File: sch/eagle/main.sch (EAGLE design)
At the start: 19 parts, among them IC1 LM339N

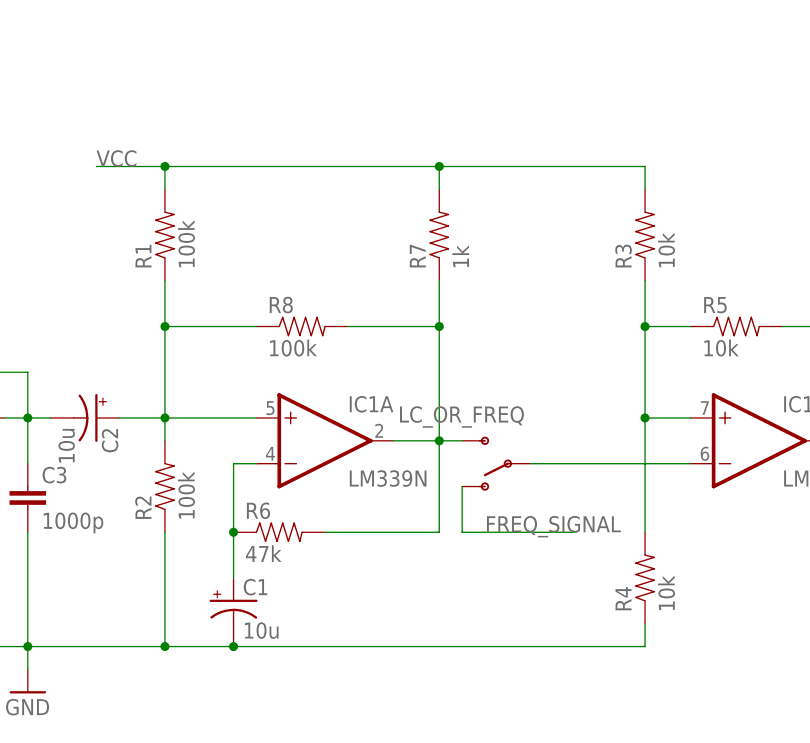
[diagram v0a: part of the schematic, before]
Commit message: [ update ] add missing power connections to lm339
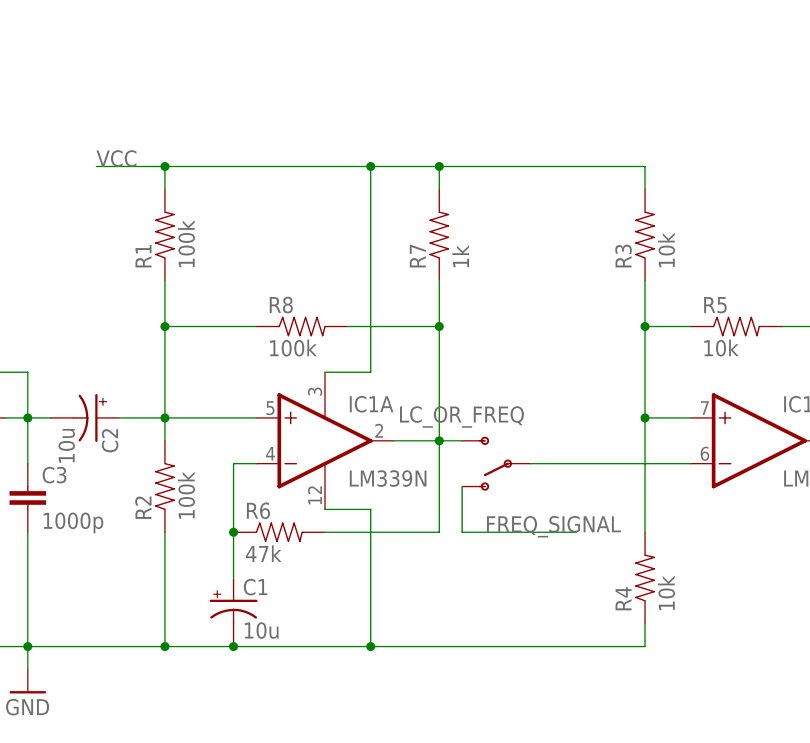
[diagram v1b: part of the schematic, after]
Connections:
- net GND: now also IC1P.GND
- net VCC: now also IC1P.V+
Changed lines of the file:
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@@
 <instance part="FREQ_CON" gate="G$1" x="0" y="93.98"/>
 <instance part="OSC_OUT" gate="G$1" x="0" y="81.28"/>
+<instance part="IC1" gate="P" x="83.82" y="66.04"/>
 </instances>
 <busses>
@@
 <pinref part="GND2" gate="1" pin="GND"/>
 <wire x1="50.8" y1="43.18" x2="50.8" y2="40.64" width="0.1524" layer="91"/>
-<wire x1="73.66" y1="43.18" x2="119.38" y2="43.18" width="0.1524" layer="91"/>
+<wire x1="73.66" y1="43.18" x2="88.9" y2="43.18" width="0.1524" layer="91"/>
 <junction x="73.66" y="43.18"/>
 <pinref part="R4" gate="G$1" pin="1"/>
+<wire x1="88.9" y1="43.18" x2="119.38" y2="43.18" width="0.1524" layer="91"/>
 <wire x1="119.38" y1="45.72" x2="119.38" y2="43.18" width="0.1524" layer="91"/>
+<pinref part="IC1" gate="P" pin="GND"/>
+<wire x1="83.82" y1="58.42" x2="88.9" y2="58.42" width="0.1524" layer="91"/>
+<wire x1="88.9" y1="58.42" x2="88.9" y2="43.18" width="0.1524" layer="91"/>
+<junction x="88.9" y="43.18"/>
 </segment>
 </net>
@@
 <wire x1="66.04" y1="96.52" x2="58.42" y2="96.52" width="0.1524" layer="91"/>
 <label x="58.42" y="96.52" size="1.778" layer="95"/>
-<wire x1="66.04" y1="96.52" x2="96.52" y2="96.52" width="0.1524" layer="91"/>
+<wire x1="66.04" y1="96.52" x2="88.9" y2="96.52" width="0.1524" layer="91"/>
 <junction x="66.04" y="96.52"/>
 <pinref part="R7" gate="G$1" pin="2"/>
+<wire x1="88.9" y1="96.52" x2="96.52" y2="96.52" width="0.1524" layer="91"/>
 <wire x1="96.52" y1="96.52" x2="96.52" y2="93.98" width="0.1524" layer="91"/>
 <wire x1="96.52" y1="96.52" x2="119.38" y2="96.52" width="0.1524" layer="91"/>
@@
 <pinref part="R3" gate="G$1" pin="2"/>
 <wire x1="119.38" y1="96.52" x2="119.38" y2="93.98" width="0.1524" layer="91"/>
+<pinref part="IC1" gate="P" pin="V+"/>
+<wire x1="83.82" y1="73.66" x2="88.9" y2="73.66" width="0.1524" layer="91"/>
+<wire x1="88.9" y1="73.66" x2="88.9" y2="96.52" width="0.1524" layer="91"/>
+<junction x="88.9" y="96.52"/>
 </segment>
 </net>

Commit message: [ update ] eagle, mcu_con
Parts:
- removed OSC_OUT: M01PTH, SparkFun:M01PTH
- added MCU_CON: (no value), SparkFun:M02PTH
- renumbered LC_OR_FREQ to FREQ_SWITCH, L_OR_C to LC_SWITCH
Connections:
- removed net LC_SENSE: LC_SWITCH.6
- removed net OSC_OUT: IC1B.OUT, OSC_OUT.1, R5.2
- new net MCU_FREQ: IC1B.OUT, MCU_CON.2, R5.2
- new net MCU_LC_SENSE: LC_SWITCH.6, MCU_CON.1
- net C: now also C2.-, C3.1, L1.2, LC_SWITCH.1; no longer L1.1, LC_SWITCH.3, LC_SWITCH.4
- net L: now also L1.1, LC_SWITCH.3, LC_SWITCH.4; no longer C2.-, C3.1, L1.2, LC_SWITCH.1
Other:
- note removed: "arduino pin2"
- note removed: "arduino pin5"
- moved on the sheet: FREQ_CON, POWER_CON
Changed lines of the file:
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@@
 <part name="C3" library="SparkFun" deviceset="CAP" device="KIT" value="1000p"/>
 <part name="L1" library="rcl" deviceset="L-EU" device="0207/10" value="221u"/>
-<part name="LC_OR_FREQ" library="SparkFun" deviceset="SWITCH-SPST" device="PTH"/>
-<part name="L_OR_C" library="SparkFun" deviceset="SWITCH-DPDT" device="EG2211"/>
+<part name="FREQ_SWITCH" library="SparkFun" deviceset="SWITCH-SPST" device="PTH"/>
+<part name="LC_SWITCH" library="SparkFun" deviceset="SWITCH-DPDT" device="EG2211"/>
 <part name="GND1" library="SparkFun" deviceset="GND" device=""/>
 <part name="SUPPLY1" library="supply2" deviceset="VCC" device=""/>
@@
 <part name="GND2" library="SparkFun" deviceset="GND" device=""/>
 <part name="FREQ_CON" library="SparkFun" deviceset="M01" device="PTH"/>
-<part name="OSC_OUT" library="SparkFun" deviceset="M01" device="PTH"/>
+<part name="MCU_CON" library="SparkFun" deviceset="M02" device="PTH"/>
 </parts>
 <sheets>
 <sheet>
 <plain>
-<text x="27.94" y="58.42" size="1.778" layer="91">arduino pin2</text>
-<text x="149.86" y="60.96" size="1.778" layer="91">arduino pin5</text>
 </plain>
 <instances>
@@
 <instance part="C3" gate="G$1" x="50.8" y="58.42"/>
 <instance part="L1" gate="G$1" x="43.18" y="68.58" rot="R90"/>
-<instance part="LC_OR_FREQ" gate="1" x="104.14" y="63.5" rot="R180"/>
-<instance part="L_OR_C" gate="G$1" x="17.78" y="68.58"/>
-<instance part="GND1" gate="1" x="15.24" y="101.6"/>
-<instance part="SUPPLY1" gate="G$1" x="15.24" y="109.22"/>
-<instance part="POWER_CON" gate="G$1" x="0" y="104.14"/>
+<instance part="FREQ_SWITCH" gate="1" x="104.14" y="63.5" rot="R180"/>
+<instance part="LC_SWITCH" gate="G$1" x="17.78" y="68.58"/>
+<instance part="GND1" gate="1" x="15.24" y="109.22"/>
+<instance part="SUPPLY1" gate="G$1" x="15.24" y="116.84"/>
+<instance part="POWER_CON" gate="G$1" x="0" y="111.76"/>
 <instance part="LC_CON" gate="G$1" x="0" y="66.04"/>
 <instance part="R8" gate="G$1" x="81.28" y="78.74"/>
 <instance part="GND2" gate="1" x="50.8" y="38.1"/>
-<instance part="FREQ_CON" gate="G$1" x="0" y="93.98"/>
-<instance part="OSC_OUT" gate="G$1" x="0" y="81.28"/>
+<instance part="FREQ_CON" gate="G$1" x="0" y="83.82"/>
 <instance part="IC1" gate="P" x="83.82" y="66.04"/>
+<instance part="MCU_CON" gate="G$1" x="0" y="96.52"/>
 </instances>
 <busses>
@@
 <segment>
 <pinref part="POWER_CON" gate="G$1" pin="1"/>
-<wire x1="7.62" y1="104.14" x2="15.24" y2="104.14" width="0.1524" layer="91"/>
+<wire x1="7.62" y1="111.76" x2="15.24" y2="111.76" width="0.1524" layer="91"/>
 <pinref part="GND1" gate="1" pin="GND"/>
 </segment>
@@
 <pinref part="LC_CON" gate="G$1" pin="1"/>
 <wire x1="7.62" y1="66.04" x2="7.62" y2="63.5" width="0.1524" layer="91"/>
-<pinref part="L_OR_C" gate="G$1" pin="5"/>
+<pinref part="LC_SWITCH" gate="G$1" pin="5"/>
 <wire x1="7.62" y1="63.5" x2="12.7" y2="63.5" width="0.1524" layer="91"/>
 <wire x1="7.62" y1="63.5" x2="7.62" y2="43.18" width="0.1524" layer="91"/>
@@
 <pinref part="POWER_CON" gate="G$1" pin="2"/>
 <pinref part="SUPPLY1" gate="G$1" pin="VCC"/>
-<wire x1="7.62" y1="106.68" x2="15.24" y2="106.68" width="0.1524" layer="91"/>
+<wire x1="7.62" y1="114.3" x2="15.24" y2="114.3" width="0.1524" layer="91"/>
 </segment>
 <segment>
@@
 <net name="C" class="0">
 <segment>
-<pinref part="L_OR_C" gate="G$1" pin="3"/>
-<wire x1="22.86" y1="68.58" x2="25.4" y2="68.58" width="0.1524" layer="91"/>
-<wire x1="25.4" y1="68.58" x2="25.4" y2="66.04" width="0.1524" layer="91"/>
-<pinref part="L_OR_C" gate="G$1" pin="4"/>
-<wire x1="25.4" y1="66.04" x2="22.86" y2="66.04" width="0.1524" layer="91"/>
-<pinref part="L1" gate="G$1" pin="1"/>
-<wire x1="25.4" y1="68.58" x2="38.1" y2="68.58" width="0.1524" layer="91"/>
-<junction x="25.4" y="68.58"/>
-<label x="22.86" y="68.58" size="1.778" layer="95"/>
-</segment>
-</net>
-<net name="L" class="0">
-<segment>
 <pinref part="L1" gate="G$1" pin="2"/>
 <pinref part="C2" gate="G$1" pin="-"/>
@@
 <wire x1="50.8" y1="63.5" x2="50.8" y2="68.58" width="0.1524" layer="91"/>
 <junction x="50.8" y="68.58"/>
-<pinref part="L_OR_C" gate="G$1" pin="1"/>
+<pinref part="LC_SWITCH" gate="G$1" pin="1"/>
 <wire x1="22.86" y1="73.66" x2="50.8" y2="73.66" width="0.1524" layer="91"/>
 <wire x1="50.8" y1="73.66" x2="50.8" y2="68.58" width="0.1524" layer="91"/>
@@
 <pinref part="LC_CON" gate="G$1" pin="2"/>
 <wire x1="7.62" y1="68.58" x2="7.62" y2="71.12" width="0.1524" layer="91"/>
-<pinref part="L_OR_C" gate="G$1" pin="2"/>
+<pinref part="LC_SWITCH" gate="G$1" pin="2"/>
 <wire x1="7.62" y1="71.12" x2="12.7" y2="71.12" width="0.1524" layer="91"/>
-</segment>
-</net>
-<net name="LC_SENSE" class="0">
-<segment>
-<pinref part="L_OR_C" gate="G$1" pin="6"/>
-<wire x1="22.86" y1="60.96" x2="33.02" y2="60.96" width="0.1524" layer="91"/>
-<label x="27.94" y="60.96" size="1.778" layer="95"/>
 </segment>
 </net>
@@
 <wire x1="96.52" y1="55.88" x2="96.52" y2="66.04" width="0.1524" layer="91"/>
 <junction x="96.52" y="66.04"/>
-<pinref part="LC_OR_FREQ" gate="1" pin="S"/>
+<pinref part="FREQ_SWITCH" gate="1" pin="S"/>
 <wire x1="96.52" y1="66.04" x2="99.06" y2="66.04" width="0.1524" layer="91"/>
 </segment>
@@
 <segment>
 <pinref part="FREQ_CON" gate="G$1" pin="1"/>
-<wire x1="7.62" y1="93.98" x2="15.24" y2="93.98" width="0.1524" layer="91"/>
-<label x="7.62" y="93.98" size="1.778" layer="95"/>
+<wire x1="7.62" y1="83.82" x2="15.24" y2="83.82" width="0.1524" layer="91"/>
+<label x="7.62" y="83.82" size="1.778" layer="95"/>
 </segment>
 <segment>
 <pinref part="IC1" gate="B" pin="-IN"/>
 <wire x1="106.68" y1="63.5" x2="124.46" y2="63.5" width="0.1524" layer="91"/>
-<pinref part="LC_OR_FREQ" gate="1" pin="P"/>
-</segment>
-<segment>
-<pinref part="LC_OR_FREQ" gate="1" pin="O"/>
+<pinref part="FREQ_SWITCH" gate="1" pin="P"/>
+</segment>
+<segment>
+<pinref part="FREQ_SWITCH" gate="1" pin="O"/>
 <wire x1="99.06" y1="60.96" x2="99.06" y2="55.88" width="0.1524" layer="91"/>
 <wire x1="99.06" y1="55.88" x2="111.76" y2="55.88" width="0.1524" layer="91"/>
@@
 </segment>
 </net>
-<net name="OSC_OUT" class="0">
-<segment>
-<pinref part="OSC_OUT" gate="G$1" pin="1"/>
-<wire x1="7.62" y1="81.28" x2="15.24" y2="81.28" width="0.1524" layer="91"/>
-<label x="7.62" y="81.28" size="1.778" layer="95"/>
-</segment>
+<net name="MCU_FREQ" class="0">
 <segment>
 <pinref part="R5" gate="G$1" pin="2"/>
@@
 <label x="147.32" y="66.04" size="1.778" layer="95"/>
 </segment>
-</net>
+<segment>
+<pinref part="MCU_CON" gate="G$1" pin="2"/>
+<wire x1="7.62" y1="99.06" x2="15.24" y2="99.06" width="0.1524" layer="91"/>
+<label x="7.62" y="99.06" size="1.778" layer="95"/>
+</segment>
+</net>
+<net name="MCU_LC_SENSE" class="0">
+<segment>
+<pinref part="LC_SWITCH" gate="G$1" pin="6"/>
+<wire x1="22.86" y1="60.96" x2="33.02" y2="60.96" width="0.1524" layer="91"/>
+<label x="27.94" y="60.96" size="1.778" layer="95"/>
+</segment>
+<segment>
+<pinref part="MCU_CON" gate="G$1" pin="1"/>
+<wire x1="7.62" y1="96.52" x2="15.24" y2="96.52" width="0.1524" layer="91"/>
+<label x="7.62" y="96.52" size="1.778" layer="95"/>
+</segment>
+</net>
+<net name="L" class="0">
+<segment>
+<pinref part="LC_SWITCH" gate="G$1" pin="3"/>
+<wire x1="22.86" y1="68.58" x2="25.4" y2="68.58" width="0.1524" layer="91"/>
+<wire x1="25.4" y1="68.58" x2="25.4" y2="66.04" width="0.1524" layer="91"/>
+<pinref part="LC_SWITCH" gate="G$1" pin="4"/>
+<wire x1="25.4" y1="66.04" x2="22.86" y2="66.04" width="0.1524" layer="91"/>
+<pinref part="L1" gate="G$1" pin="1"/>
+<wire x1="25.4" y1="68.58" x2="38.1" y2="68.58" width="0.1524" layer="91"/>
+<junction x="25.4" y="68.58"/>
+<label x="22.86" y="68.58" size="1.778" layer="95"/>
+</segment>
+</net>

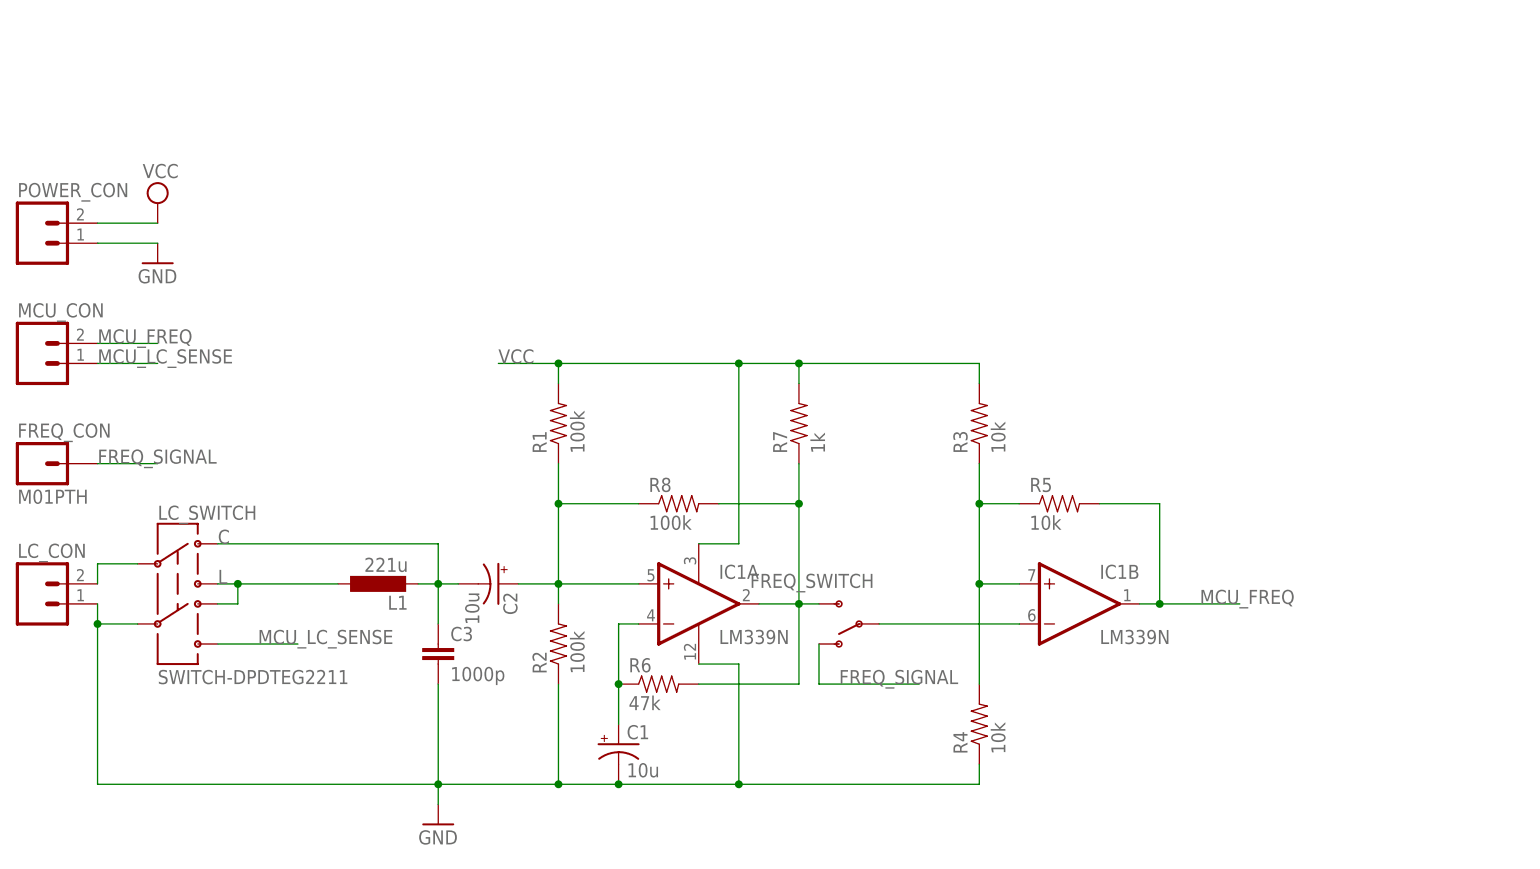
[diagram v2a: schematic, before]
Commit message: [ update ] eagle, switch connectors
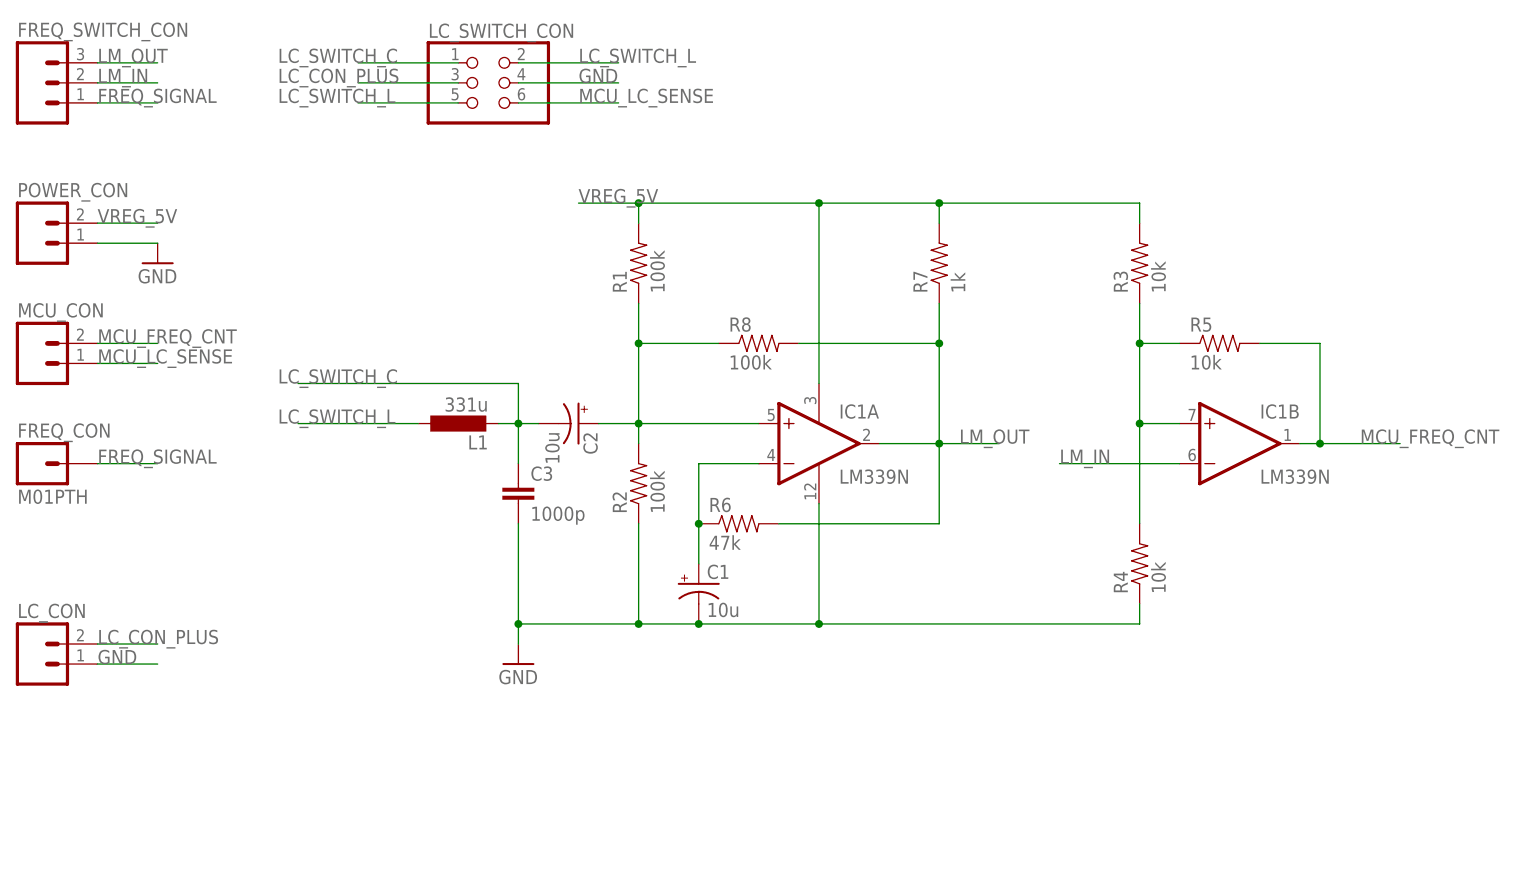
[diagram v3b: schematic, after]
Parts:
- removed FREQ_SWITCH: (no value), SparkFun:SWITCH-SPSTPTH
- removed LC_SWITCH: SWITCH-DPDTEG2211, SparkFun:SWITCH-DPDTEG2211
- added FREQ_SWITCH_CON: (no value), SparkFun:M03PTH
- added LC_SWITCH_CON: (no value), SparkFun:PINHD-2X3
- L1: value 221u -> 331u
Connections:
- net MCU_FREQ renamed MCU_FREQ_CNT
- net VCC renamed VREG_5V
- removed net C: C2.-, C3.1, L1.2, LC_SWITCH.1
- removed net L: L1.1, LC_SWITCH.3, LC_SWITCH.4
- removed net N$1: FREQ_SWITCH.S, IC1A.OUT, R6.2, R7.1, R8.2
- removed net N$3: LC_CON.2, LC_SWITCH.2
- new net LC_CON_PLUS: LC_CON.2, LC_SWITCH_CON.3
- new net LC_SWITCH_C: C2.-, C3.1, L1.2, LC_SWITCH_CON.1
- new net LC_SWITCH_L: L1.1, LC_SWITCH_CON.2, LC_SWITCH_CON.5
- new net LM_IN: FREQ_SWITCH_CON.2, IC1B.-IN
- new net LM_OUT: FREQ_SWITCH_CON.3, IC1A.OUT, R6.2, R7.1, R8.2
- net FREQ_SIGNAL: now also FREQ_SWITCH_CON.1; no longer FREQ_SWITCH.O, FREQ_SWITCH.P, IC1B.-IN
- net GND: now also LC_SWITCH_CON.4; no longer LC_SWITCH.5
- net MCU_LC_SENSE: now also LC_SWITCH_CON.6; no longer LC_SWITCH.6
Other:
- note added: "LC stage: Ls in series or Cs in parallel"
- note added: "oscillator stage"
- note added: "schmitt trigger stage"
- moved on the sheet: C1, C2, C3, IC1A, IC1B, L1, LC_CON, R1, R2, R3, R4, R5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

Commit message: [ add ] eagle, board routed. to refine.
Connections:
- net LC_SWITCH_L: now also LC_SWITCH_CON.6; no longer LC_SWITCH_CON.2
- net MCU_LC_SENSE: now also LC_SWITCH_CON.2; no longer LC_SWITCH_CON.6
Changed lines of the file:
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@@
 </segment>
 <segment>
-<pinref part="LC_SWITCH_CON" gate="A" pin="6"/>
-<wire x1="60.96" y1="129.54" x2="73.66" y2="129.54" width="0.1524" layer="91"/>
-<label x="68.58" y="129.54" size="1.778" layer="95"/>
+<pinref part="LC_SWITCH_CON" gate="A" pin="2"/>
+<wire x1="60.96" y1="134.62" x2="73.66" y2="134.62" width="0.1524" layer="91"/>
+<label x="68.58" y="134.62" size="1.778" layer="95"/>
 </segment>
 </net>
@@
 </segment>
 <segment>
-<pinref part="LC_SWITCH_CON" gate="A" pin="2"/>
-<wire x1="60.96" y1="134.62" x2="73.66" y2="134.62" width="0.1524" layer="91"/>
-<label x="68.58" y="134.62" size="1.778" layer="95"/>
-</segment>
-<segment>
 <pinref part="L1" gate="G$1" pin="1"/>
 <wire x1="33.02" y1="88.9" x2="48.26" y2="88.9" width="0.1524" layer="91"/>
 <label x="30.48" y="88.9" size="1.778" layer="95"/>
 </segment>
+<segment>
+<pinref part="LC_SWITCH_CON" gate="A" pin="6"/>
+<wire x1="60.96" y1="129.54" x2="73.66" y2="129.54" width="0.1524" layer="91"/>
+<label x="68.58" y="129.54" size="1.778" layer="95"/>
+</segment>
 </net>
